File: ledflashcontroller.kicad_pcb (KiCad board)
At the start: 2 copper layers, 100 x 100 mm, 72 parts, among them J1 Conn_02x08_Odd_Even, J2 CONN_01X02, J3 CONN_01X02, J4 Conn_01x02, K1 LDD-1000H, K2 LDD-1000H, P1 V_IN, P10 BNC, P11 BNC, P12 BNC, P2 I2C_HEADER, P3 GPIO_HEADER, P4 V_DIM1, P5 V_DIM2, P6 V_OUT, P7 BNC, P8 BNC, P9 BNC, Q1 IRLML6244, Q2 IRFB3256, U1 Teensy3.6_no-center, U10 DMC2700, U11 DS3231, U2 ISO1540, U3 DMC2700, U4 DMC2700, U5 ISO1540, U6 DMC2700, U7 DMC2700, U8 ISO1540, U9 DMC2700

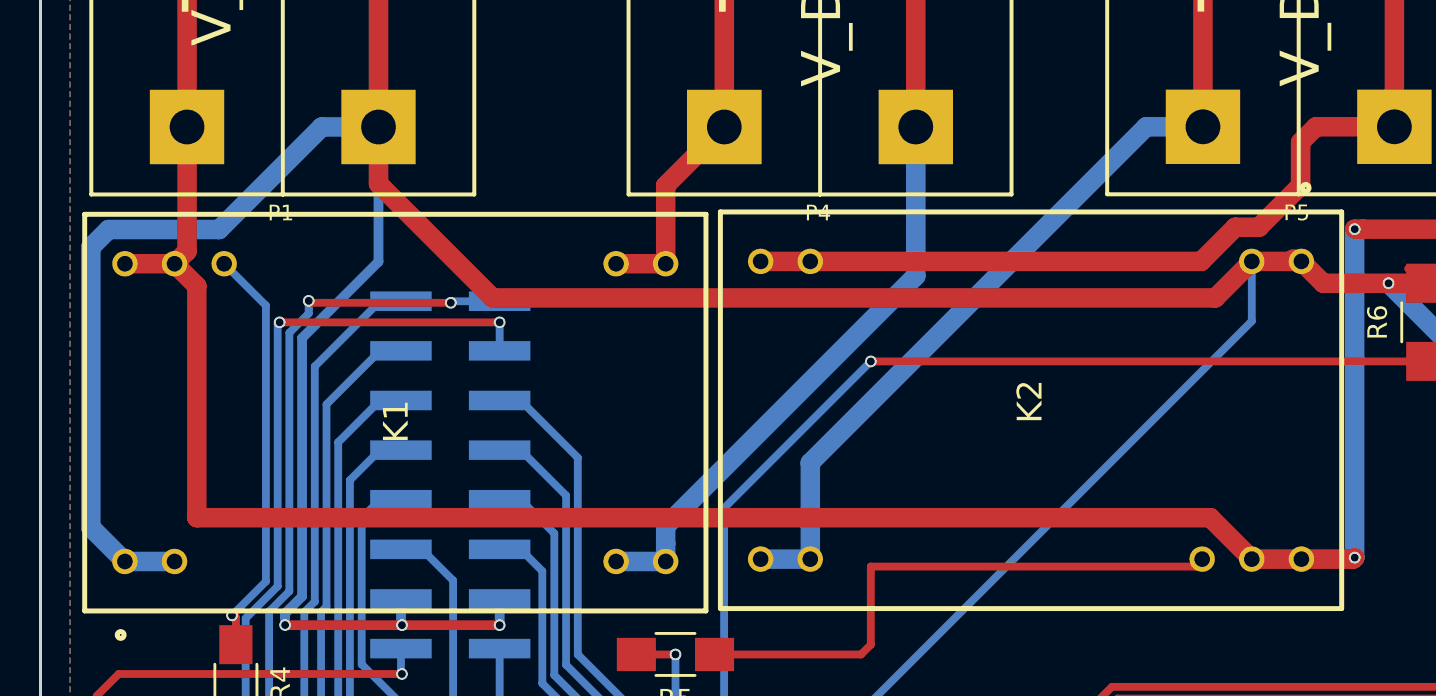
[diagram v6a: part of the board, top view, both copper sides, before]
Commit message: Correct and add new LDD footprint to pcb
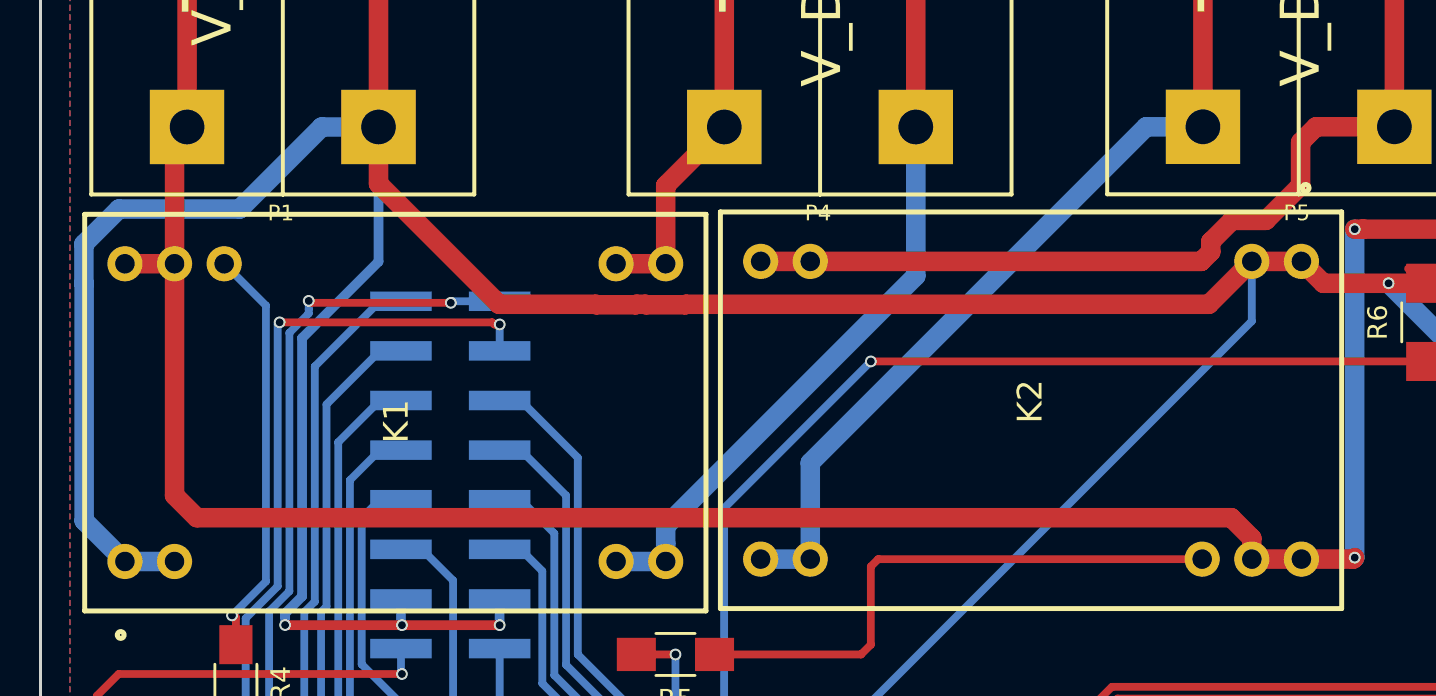
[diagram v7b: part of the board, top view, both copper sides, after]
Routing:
- net GND: track 770.3 -> 771.2 mm
- net +48V: track 150.5 -> 151.2 mm
- net Net-(K2-Pad22): track 29.4 -> 29.9 mm

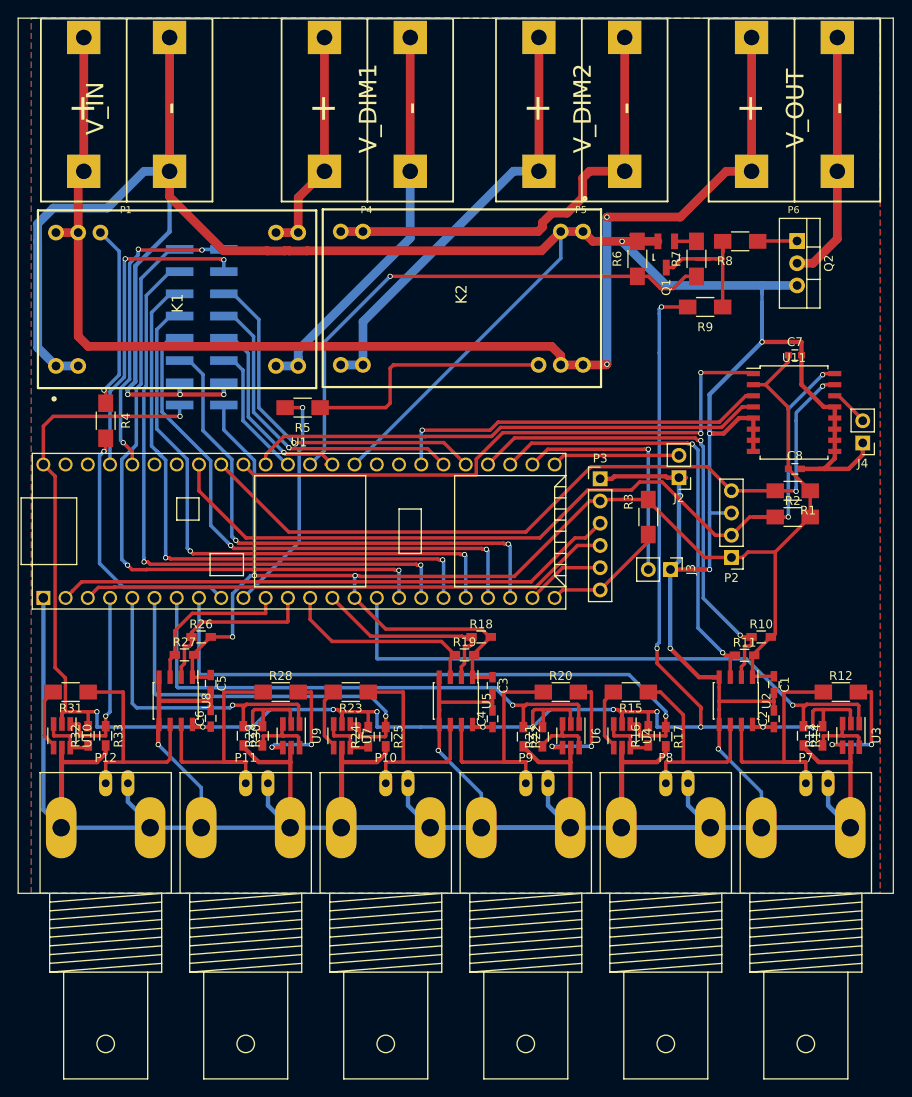
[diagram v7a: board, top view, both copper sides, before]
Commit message: Switched RTC_SQW and RTC_32kHz for improved routing
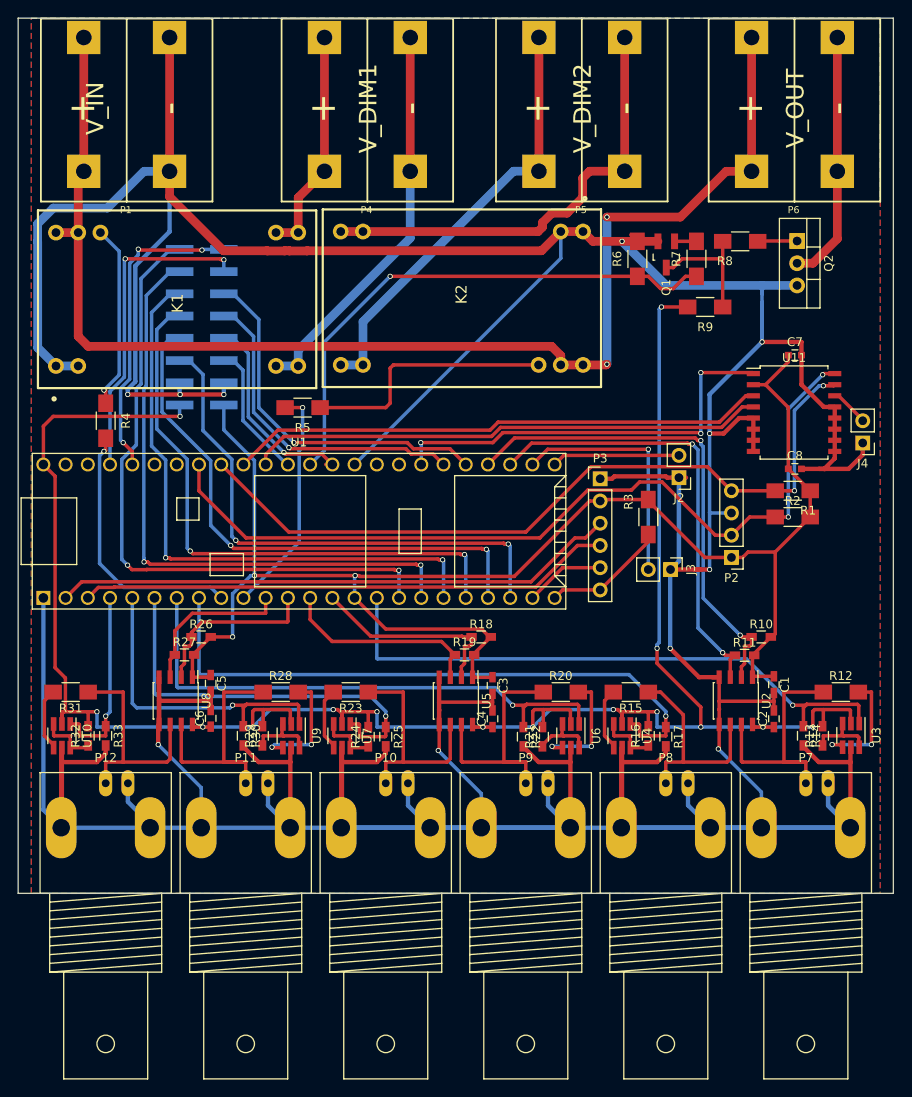
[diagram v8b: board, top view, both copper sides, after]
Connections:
- U1 pad 36: /RTC_SQW -> /RTC_32kHz
- U1 pad 44: /RTC_32kHz -> /RTC_SQW
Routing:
- net /RTC_32kHz: track 68.8 -> 48.1 mm, vias 2 -> 3
- net /RTC_SQW: track 43.5 -> 61.5 mm, vias 1 -> 0
- net Net-(Q1-Pad3): track 17.1 -> 14.4 mm
- net /SCL: track 100.4 -> 97.9 mm
- net /TRIG_PU8: track 69.6 -> 68.9 mm
